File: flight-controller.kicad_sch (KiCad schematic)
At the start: 18 parts, among them J1 XT60PW-M, U1 ACS773LCB-100B-PFF, U2 LMR33630ADDA

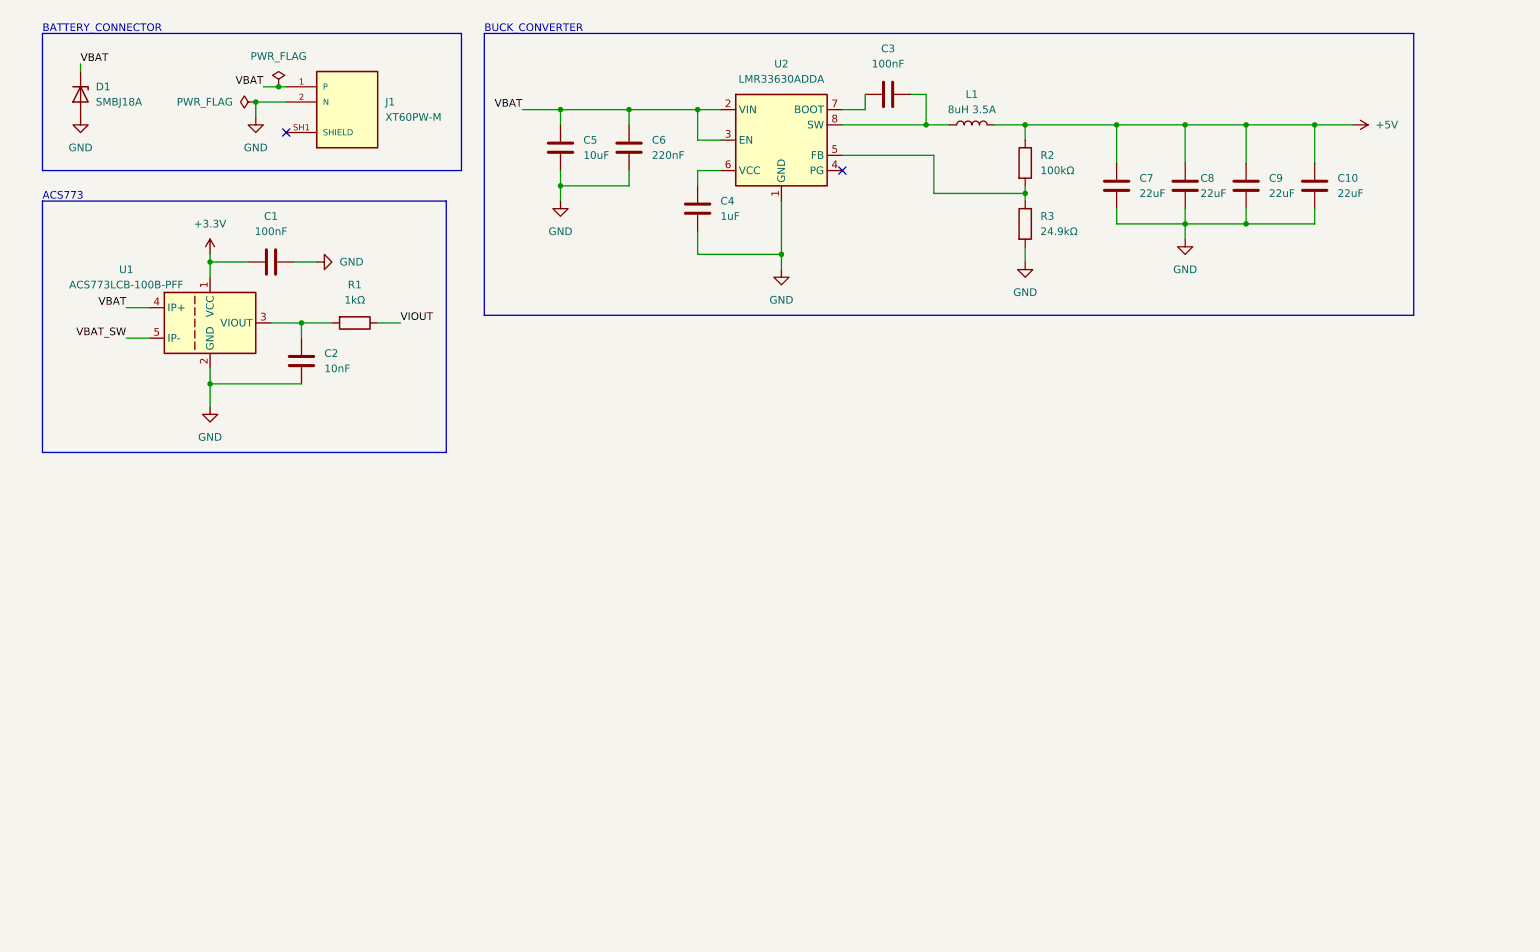
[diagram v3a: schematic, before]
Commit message: feat: Added LDO
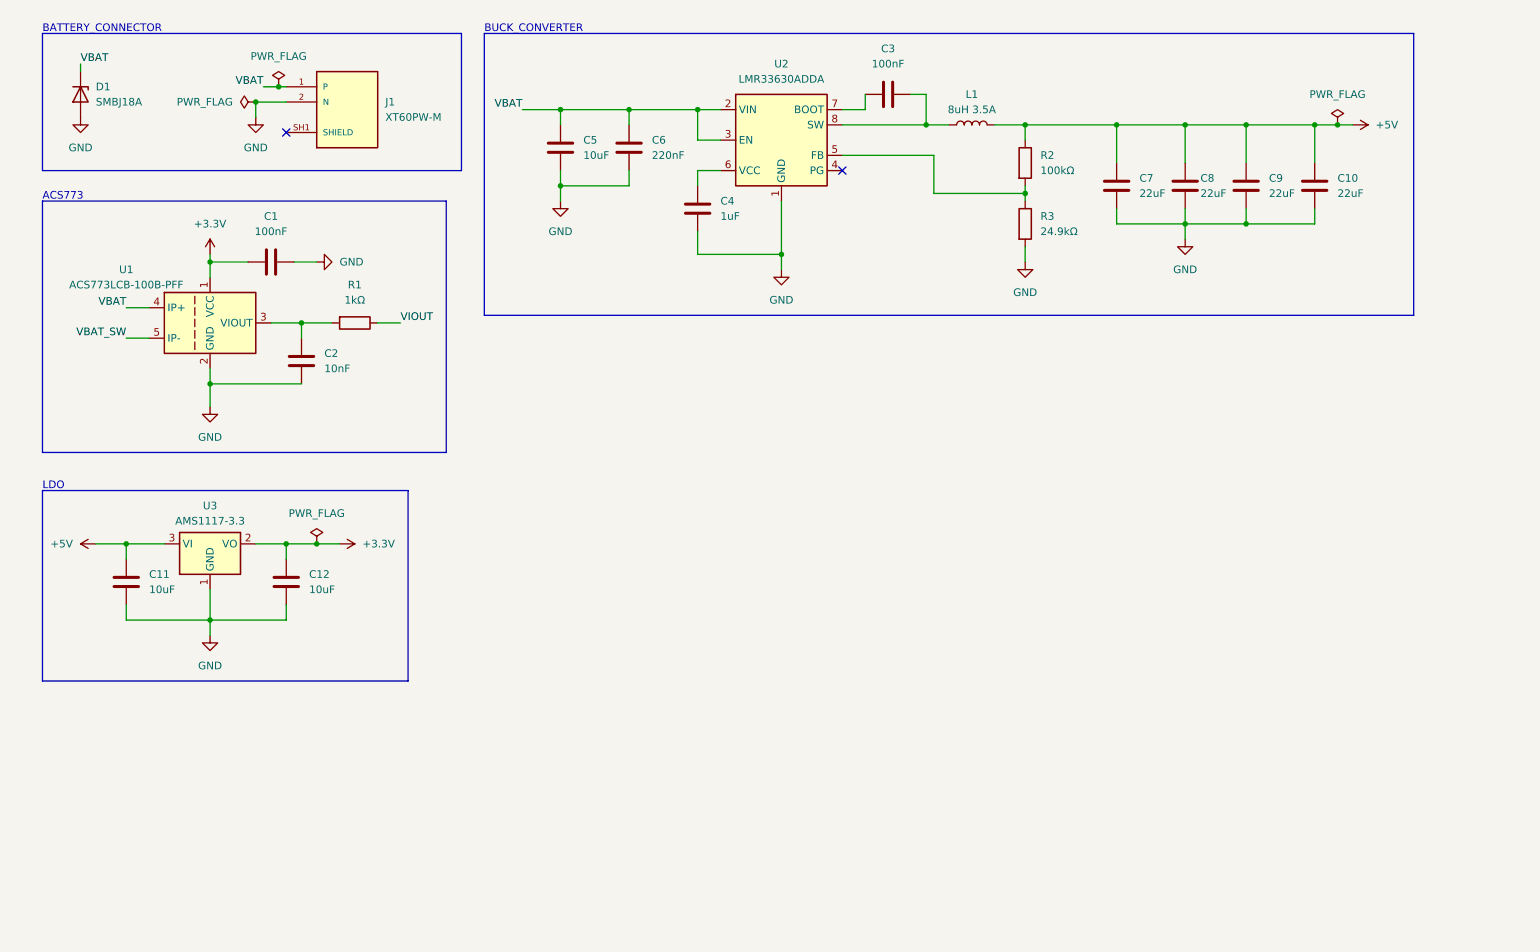
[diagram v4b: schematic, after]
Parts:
- added C11, C12: 10uF, Capacitor_SMD:C_1206_3216Metric, symbol Device:C
- added U3: AMS1117-3.3, Package_TO_SOT_SMD:SOT-223-3_TabPin2, symbol Regulator_Linear:AMS1117-3.3
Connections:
- net +3.3V: now also C12.1, U3.2 (VO)
- net +5V: now also C11.1, U3.3 (VI)
- net GND: now also C11.2, C12.2, U3.1 (GND)
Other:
- note added: "LDO"

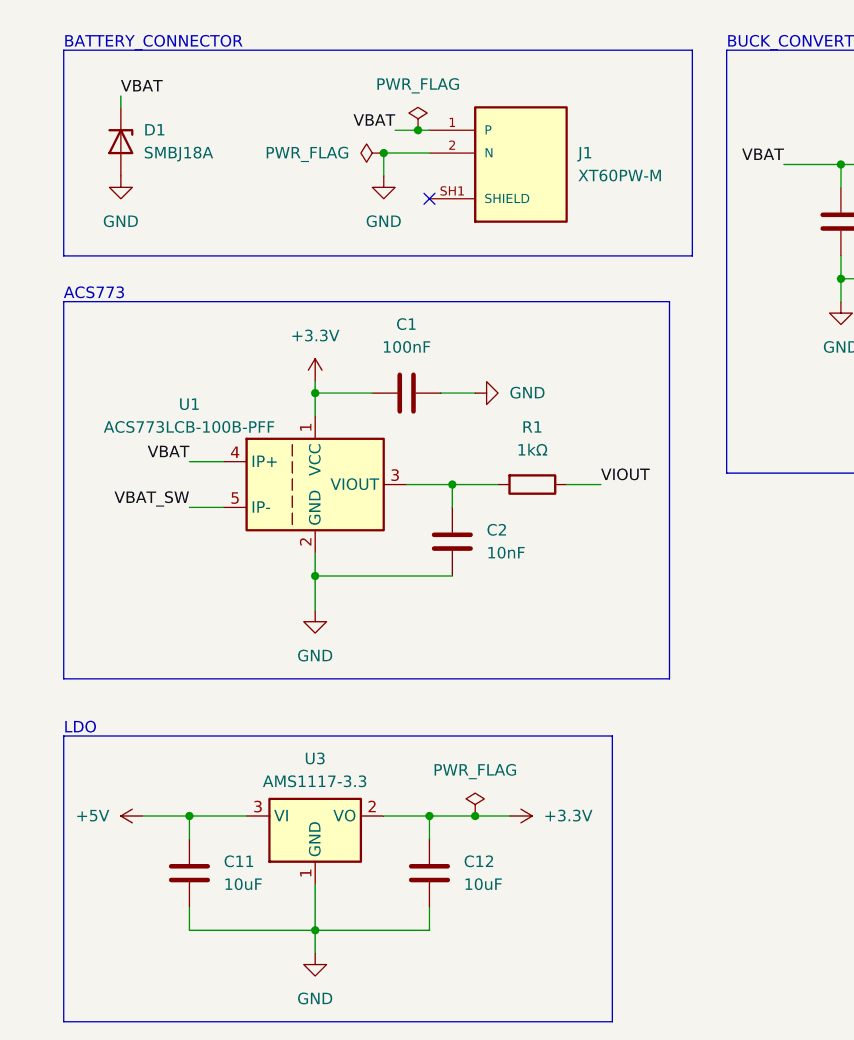
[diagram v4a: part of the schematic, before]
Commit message: fix: Fixed low pass filter for curr_sense
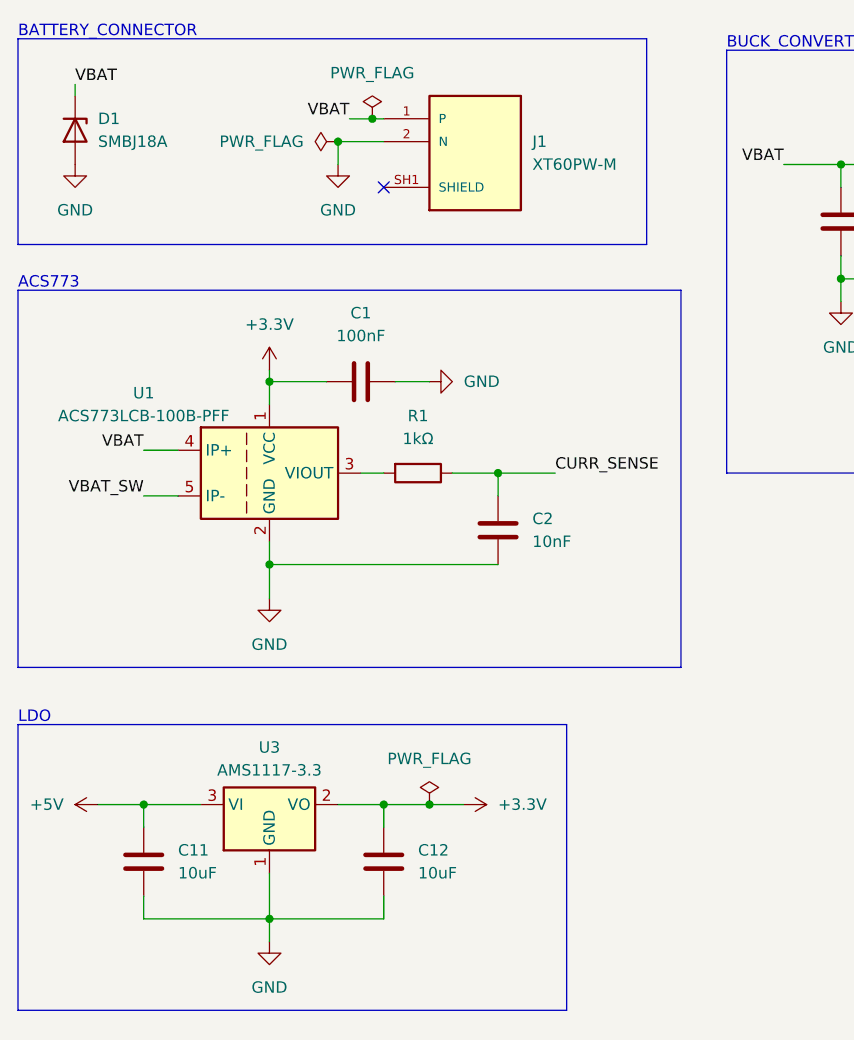
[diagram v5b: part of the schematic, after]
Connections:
- net at R1.2, U1.3 (VIOUT): no longer C2.1
- net VIOUT renamed CURR_SENSE
- net CURR_SENSE: now also C2.1
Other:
- moved on the sheet: C1, C11, C12, C2, D1, J1, R1, U1, U3

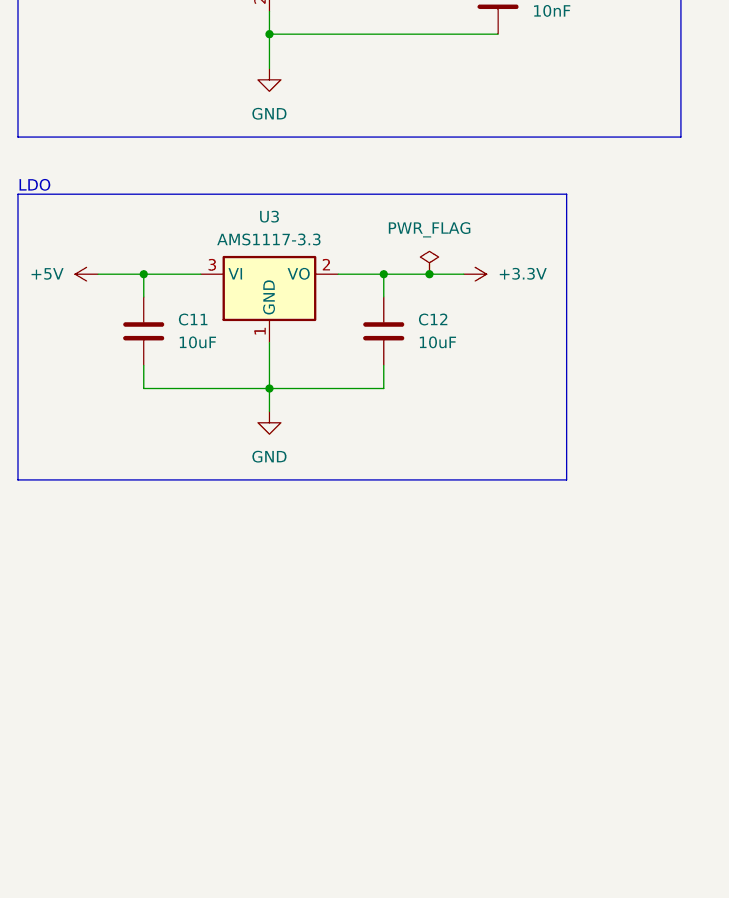
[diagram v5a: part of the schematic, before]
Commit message: feat: Added voltage divider
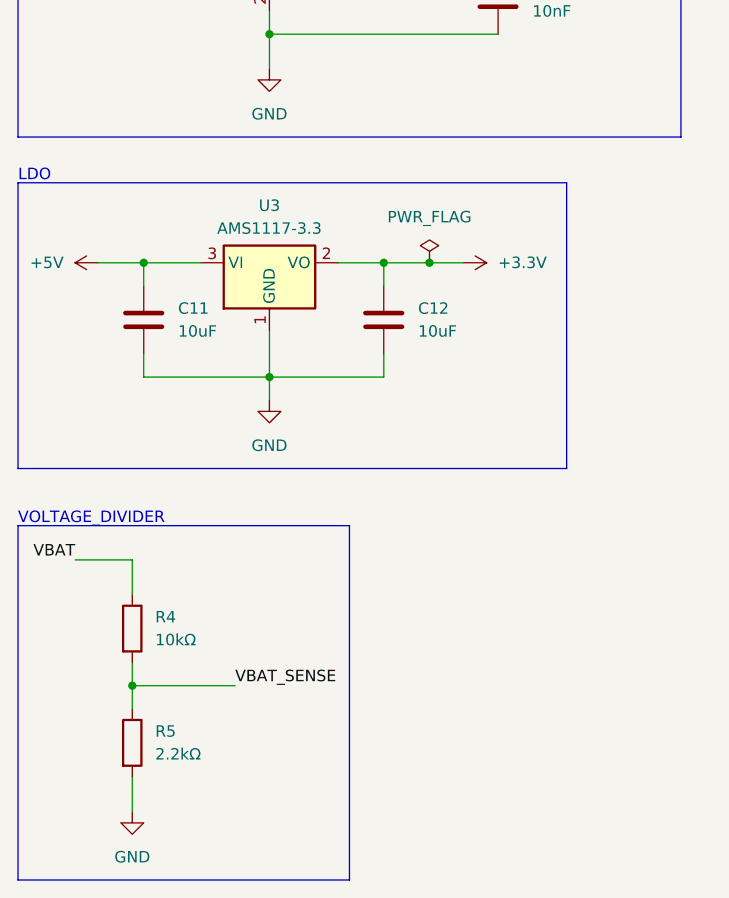
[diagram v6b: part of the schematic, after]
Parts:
- added R4: 10kΩ, Resistor_SMD:R_0805_2012Metric, symbol Device:R
- added R5: 2.2kΩ, Resistor_SMD:R_0805_2012Metric, symbol Device:R
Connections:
- net GND: now also R5.2
- net VBAT: now also R4.1
- new net VBAT_SENSE: R4.2, R5.1
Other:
- note added: "VOLTAGE_DIVIDER"
- moved on the sheet: C11, C12, U3

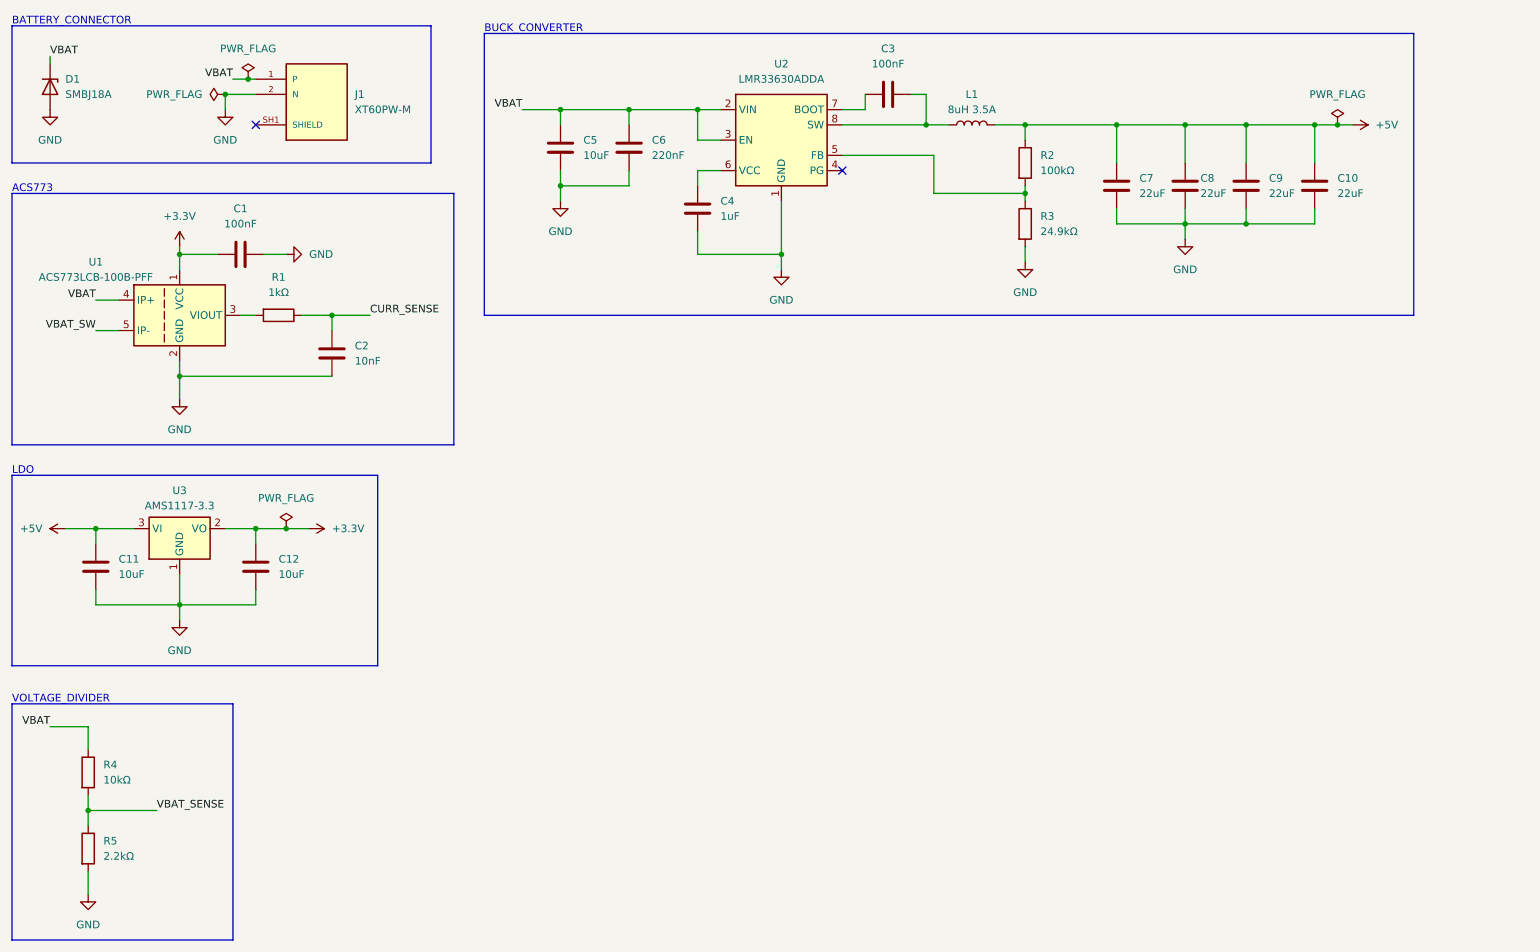
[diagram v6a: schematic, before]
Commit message: feat: Added ESC connectors
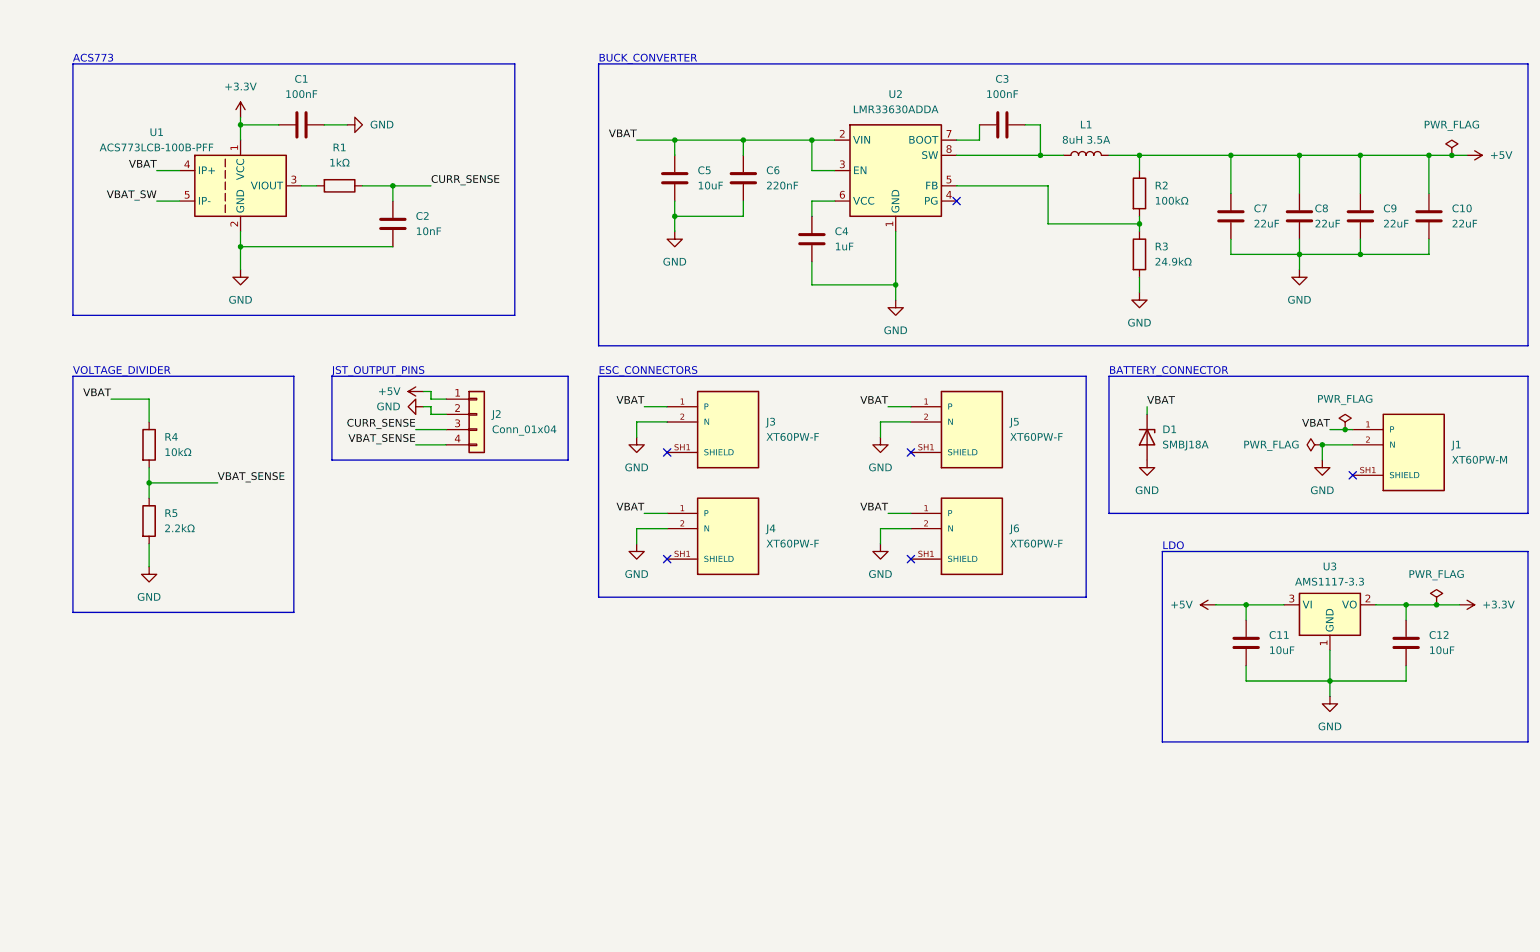
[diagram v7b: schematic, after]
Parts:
- added J2: Conn_01x04, Connector_JST:JST_XH_B4B-XH-A_1x04_P2.50mm_Vertical, symbol Connector_Generic:Conn_01x04
- added J3, J4, J5, J6: XT60PW-F, Connector_AMASS:AMASS_XT60PW-F_1x02_P7.20mm_Horizontal, symbol Custom_BEC_PS:XT60PW-M
- J1: footprint XT60PW-M:AMASS_XT60PW-M -> Connector_AMASS:AMASS_XT60PW-M_1x02_P7.20mm_Horizontal
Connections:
- net +5V: now also J2.1 (Pin_1)
- net CURR_SENSE: now also J2.3 (Pin_3)
- net GND: now also J2.2 (Pin_2), J3.2 (N), J4.2 (N), J5.2 (N), J6.2 (N)
- net VBAT: now also J3.1 (P), J4.1 (P), J5.1 (P), J6.1 (P)
- net VBAT_SENSE: now also J2.4 (Pin_4)
- new net: J4.SH1 (SHIELD), J4.SH2 (SHIELD)
- new net: J6.SH1 (SHIELD), J6.SH2 (SHIELD)
- new net: J5.SH1 (SHIELD), J5.SH2 (SHIELD)
- new net: J3.SH1 (SHIELD), J3.SH2 (SHIELD)
- no-connect marks 2 -> 6
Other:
- note added: "ESC_CONNECTORS"
- note added: "JST_OUTPUT_PINS"
- moved on the sheet: C1, C10, C11, C12, C2, C3, C4, C5, C6, C7, C8, C9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
